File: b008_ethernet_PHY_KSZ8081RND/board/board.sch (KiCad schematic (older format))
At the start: 21 parts, among them J1 006_RMII_2x10, J2 011_GPIO_2x2, J3 009_1000BASE-T_2x5, U14 KSZ8081RND, Y1 25MhZ

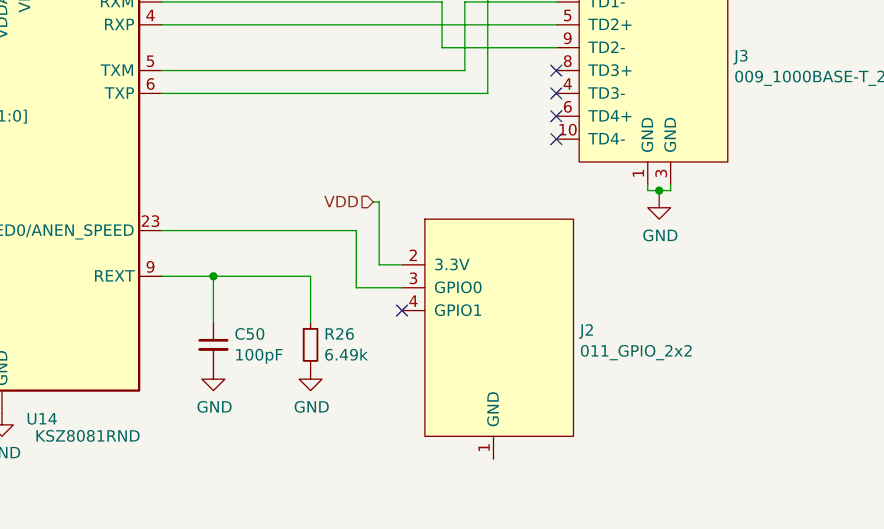
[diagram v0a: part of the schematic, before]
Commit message: added part info for silicon parts
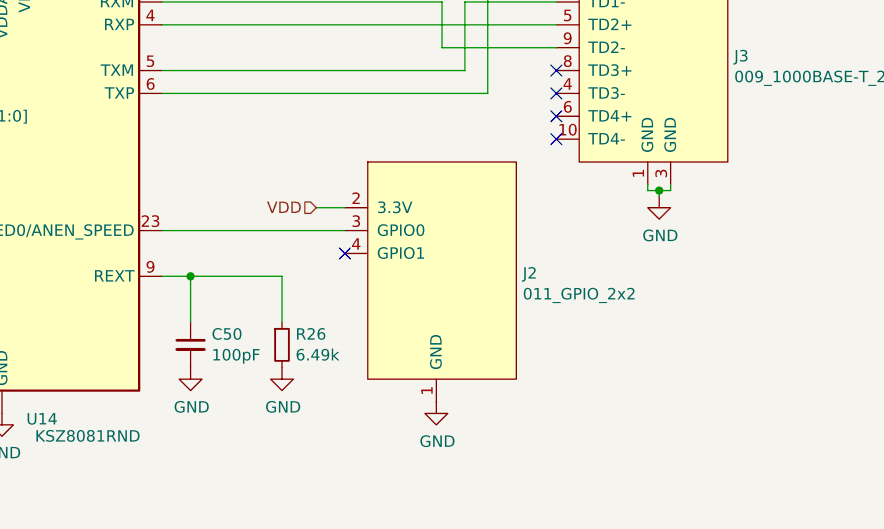
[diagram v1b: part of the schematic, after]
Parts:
- U14: MPN (none) -> KSZ8081RND
- Y1: MPN (none) -> ‎XC3065CT-ND‎
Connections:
- net GND: now also J2.1 (GND)
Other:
- moved on the sheet: C50, J2, R26
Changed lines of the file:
@@
 F 2 "Package_DFN_QFN:QFN-24-1EP_4x4mm_P0.5mm_EP2.6x2.6mm" H 7275 2200 50  0001 C CNN
 F 3 "http://ww1.microchip.com/downloads/en/DeviceDoc/00002199A.pdf" H 3625 3400 50  0001 C CNN
+F 4 "KSZ8081RND" H 5875 3200 50  0001 C CNN "MPN"
 	1    5875 3200
 	1    0    0    -1
@@
 F 2 "Crystal:Crystal_SMD_Abracon_ABM8G-4Pin_3.2x2.5mm" H 4475 4125 50  0001 C CNN
 F 3 "~" H 4475 4125 50  0001 C CNN
+F 4 "‎XC3065CT-ND‎" H 4475 4125 50  0001 C CNN "MPN"
 	1    4475 4125
 	1    0    0    -1
@@
 L Device:C_Small C50
 U 1 1 6033379D
-P 6800 3900
-F 0 "C50" H 6892 3946 50  0000 L CNN
-F 1 "100pF" H 6892 3855 50  0000 L CNN
-F 2 "Capacitor_SMD:C_0603_1608Metric" H 6800 3900 50  0001 C CNN
-F 3 "~" H 6800 3900 50  0001 C CNN
-	1    6800 3900
+P 6700 3900
+F 0 "C50" H 6792 3946 50  0000 L CNN
+F 1 "100pF" H 6792 3855 50  0000 L CNN
+F 2 "Capacitor_SMD:C_0603_1608Metric" H 6700 3900 50  0001 C CNN
+F 3 "~" H 6700 3900 50  0001 C CNN
+	1    6700 3900
 	1    0    0    -1
 $EndComp
@@
 L power:GND #PWR0144
 U 1 1 603337A3
-P 6800 4000
-F 0 "#PWR0144" H 6800 3750 50  0001 C CNN
-F 1 "GND" H 6805 3827 50  0000 C CNN
-F 2 "" H 6800 4000 50  0001 C CNN
-F 3 "" H 6800 4000 50  0001 C CNN
-	1    6800 4000
-	1    0    0    -1
-$EndComp
-Wire Wire Line
-	6575 3600 6800 3600
-Wire Wire Line
-	6800 3600 6800 3800
+P 6700 4000
+F 0 "#PWR0144" H 6700 3750 50  0001 C CNN
+F 1 "GND" H 6705 3827 50  0000 C CNN
+F 2 "" H 6700 4000 50  0001 C CNN
+F 3 "" H 6700 4000 50  0001 C CNN
+	1    6700 4000
+	1    0    0    -1
+$EndComp
+Wire Wire Line
+	6700 3600 6700 3800
 $Comp
 L Device:R_Small R26
 U 1 1 60333C7C
-P 7225 3900
-F 0 "R26" H 7284 3946 50  0000 L CNN
-F 1 "6.49k" H 7284 3855 50  0000 L CNN
-F 2 "Resistor_SMD:R_0603_1608Metric" H 7225 3900 50  0001 C CNN
-F 3 "~" H 7225 3900 50  0001 C CNN
-	1    7225 3900
+P 7100 3900
+F 0 "R26" H 7159 3946 50  0000 L CNN
+F 1 "6.49k" H 7159 3855 50  0000 L CNN
+F 2 "Resistor_SMD:R_0603_1608Metric" H 7100 3900 50  0001 C CNN
+F 3 "~" H 7100 3900 50  0001 C CNN
+	1    7100 3900
 	1    0    0    -1
 $EndComp
@@
 L power:GND #PWR0145
 U 1 1 603340ED
-P 7225 4000
-F 0 "#PWR0145" H 7225 3750 50  0001 C CNN
-F 1 "GND" H 7230 3827 50  0000 C CNN
-F 2 "" H 7225 4000 50  0001 C CNN
-F 3 "" H 7225 4000 50  0001 C CNN
-	1    7225 4000
-	1    0    0    -1
-$EndComp
-Wire Wire Line
-	7225 3800 7225 3600
-Wire Wire Line
-	7225 3600 6800 3600
-Connection ~ 6800 3600
+P 7100 4000
+F 0 "#PWR0145" H 7100 3750 50  0001 C CNN
+F 1 "GND" H 7105 3827 50  0000 C CNN
+F 2 "" H 7100 4000 50  0001 C CNN
+F 3 "" H 7100 4000 50  0001 C CNN
+	1    7100 4000
+	1    0    0    -1
+$EndComp
+Wire Wire Line
+	7100 3800 7100 3600
 $Comp
 L Device:R_Small R22
@@
 VDD
 $Comp
-L put_on_edge:011_GPIO_2x2 J2
-U 1 1 6036615C
-P 8075 3850
-F 0 "J2" H 8403 3863 50  0000 L CNN
-F 1 "011_GPIO_2x2" H 8403 3772 50  0000 L CNN
-F 2 "on_edge:on_edge_2x02_host" H 8375 4500 50  0001 C CNN
-F 3 "" H 8375 4500 50  0001 C CNN
-	1    8075 3850
-	1    0    0    -1
-$EndComp
-$Comp
 L put_on_edge:009_1000BASE-T_2x5 J3
 U 1 1 60366BF1
@@
 Wire Wire Line
 	8750 3225 8800 3225
-Wire Wire Line
-	7425 3400 7425 3650
-Wire Wire Line
-	7425 3650 7625 3650
-Wire Wire Line
-	6575 3400 7425 3400
-Text HLabel 7500 3275 0    50   Input ~ 0
+Text HLabel 7250 3300 0    50   Input ~ 0
 VDD
-Wire Wire Line
-	7500 3275 7525 3275
-Wire Wire Line
-	7525 3275 7525 3550
-Wire Wire Line
-	7525 3550 7625 3550
-NoConn ~ 7625 3750
 $Comp
 L power:GND #PWR0103
@@
 Wire Wire Line
 	4475 3950 4475 4025
+NoConn ~ 7375 3500
+$Comp
+L put_on_edge:011_GPIO_2x2 J2
+U 1 1 6036615C
+P 7825 3600
+F 0 "J2" H 8153 3613 50  0000 L CNN
+F 1 "011_GPIO_2x2" H 8153 3522 50  0000 L CNN
+F 2 "on_edge:on_edge_2x02_host" H 8125 4250 50  0001 C CNN
+F 3 "" H 8125 4250 50  0001 C CNN
+	1    7825 3600
+	1    0    0    -1
+$EndComp
+$Comp
+L power:GND #PWR?
+U 1 1 604270D0
+P 7775 4150
+F 0 "#PWR?" H 7775 3900 50  0001 C CNN
+F 1 "GND" H 7780 3977 50  0000 C CNN
+F 2 "" H 7775 4150 50  0001 C CNN
+F 3 "" H 7775 4150 50  0001 C CNN
+	1    7775 4150
+	1    0    0    -1
+$EndComp
+Wire Wire Line
+	6575 3400 7375 3400
+Wire Wire Line
+	7250 3300 7375 3300
+Connection ~ 6700 3600
+Wire Wire Line
+	6700 3600 7100 3600
+Wire Wire Line
+	6575 3600 6700 3600
 $EndSCHEMATC

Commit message: improved b008 but not done
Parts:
- J1: symbol put_on_edge:006_RMII_2x10 -> board-rescue:006_RMII_2x10-put_on_edge
- J2: footprint on_edge:on_edge_2x02_host -> on_edge:on_edge_2x05_host; symbol put_on_edge:011_GPIO_2x2 -> put_on_edge:011_GPIO
- J3: symbol put_on_edge:009_1000BASE-T_2x5 -> put_on_edge:014_100BASE-T
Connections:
- net GND: now also J3.6 (GND); no longer J3.3 (GND)
- net VDD: now also J2.9 (3.3V); no longer J2.2 (3.3V)
- net at U14.23 (LED0/ANEN_SPEED): now also J2.2 (GPIO0); no longer J2.3 (GPIO0)
- net at U14.3 (RXM): now also J3.5 (TD2-); no longer J3.9 (TD2-)
- net at U14.4 (RXP): now also J3.4 (TD2+); no longer J3.5 (TD2+)
- net at U14.5 (TXM): now also J3.3 (TD1-); no longer J3.2 (TD1-)
- net at U14.6 (TXP): now also J3.2 (TD1+); no longer J3.7 (TD1+)
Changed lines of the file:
@@
 	6575 2400 7800 2400
 $Comp
-L put_on_edge:006_RMII_2x10 J1
+L board-rescue:006_RMII_2x10-put_on_edge J1
 U 1 1 60348143
 P 1675 2650
@@
 VDD
 $Comp
-L put_on_edge:009_1000BASE-T_2x5 J3
+L put_on_edge:014_100BASE-T J3
 U 1 1 60366BF1
-P 8750 2650
-F 0 "J3" H 9078 2663 50  0000 L CNN
-F 1 "009_1000BASE-T_2x5" H 9078 2572 50  0000 L CNN
-F 2 "on_edge:on_edge_2x05_host" H 9050 3300 50  0001 C CNN
-F 3 "" H 9050 3300 50  0001 C CNN
-	1    8750 2650
-	1    0    0    -1
-$EndComp
-Wire Wire Line
-	6575 2500 8300 2500
-Wire Wire Line
-	8300 2600 7800 2600
+P 9650 2650
+F 0 "J3" H 9978 2663 50  0000 L CNN
+F 1 "009_1000BASE-T_2x5" H 9978 2572 50  0000 L CNN
+F 2 "on_edge:on_edge_2x05_host" H 9950 3300 50  0001 C CNN
+F 3 "" H 9950 3300 50  0001 C CNN
+	1    9650 2650
+	1    0    0    -1
+$EndComp
 Wire Wire Line
 	7800 2600 7800 2400
@@
 	7900 2700 7900 2400
 Wire Wire Line
-	7900 2400 8300 2400
-Wire Wire Line
 	6575 2700 7900 2700
 Wire Wire Line
 	8000 2800 8000 2300
 Wire Wire Line
-	8000 2300 8300 2300
-Wire Wire Line
 	6575 2800 8000 2800
-NoConn ~ 8300 2700
-NoConn ~ 8300 2800
-NoConn ~ 8300 2900
-NoConn ~ 8300 3000
 $Comp
 L power:GND #PWR0102
 U 1 1 60385EA1
-P 8750 3250
-F 0 "#PWR0102" H 8750 3000 50  0001 C CNN
-F 1 "GND" H 8755 3077 50  0000 C CNN
-F 2 "" H 8750 3250 50  0001 C CNN
-F 3 "" H 8750 3250 50  0001 C CNN
-	1    8750 3250
-	1    0    0    -1
-$EndComp
-Wire Wire Line
-	8700 3200 8700 3225
-Wire Wire Line
-	8700 3225 8750 3225
-Wire Wire Line
-	8800 3225 8800 3200
-Wire Wire Line
-	8750 3250 8750 3225
-Connection ~ 8750 3225
-Wire Wire Line
-	8750 3225 8800 3225
-Text HLabel 7250 3300 0    50   Input ~ 0
+P 9650 3250
+F 0 "#PWR0102" H 9650 3000 50  0001 C CNN
+F 1 "GND" H 9655 3077 50  0000 C CNN
+F 2 "" H 9650 3250 50  0001 C CNN
+F 3 "" H 9650 3250 50  0001 C CNN
+	1    9650 3250
+	1    0    0    -1
+$EndComp
+Wire Wire Line
+	9600 3200 9600 3225
+Wire Wire Line
+	9600 3225 9650 3225
+Wire Wire Line
+	9700 3225 9700 3200
+Wire Wire Line
+	9650 3250 9650 3225
+Connection ~ 9650 3225
+Wire Wire Line
+	9650 3225 9700 3225
+Text HLabel 7825 4000 0    50   Input ~ 0
 VDD
 $Comp
@@
 Wire Wire Line
 	4475 3950 4475 4025
-NoConn ~ 7375 3500
-$Comp
-L put_on_edge:011_GPIO_2x2 J2
+NoConn ~ 7950 3500
+$Comp
+L put_on_edge:011_GPIO J2
 U 1 1 6036615C
-P 7825 3600
-F 0 "J2" H 8153 3613 50  0000 L CNN
-F 1 "011_GPIO_2x2" H 8153 3522 50  0000 L CNN
-F 2 "on_edge:on_edge_2x02_host" H 8125 4250 50  0001 C CNN
-F 3 "" H 8125 4250 50  0001 C CNN
-	1    7825 3600
-	1    0    0    -1
-$EndComp
-$Comp
-L power:GND #PWR?
+P 8400 3750
+F 0 "J2" H 8728 3763 50  0000 L CNN
+F 1 "011_GPIO_2x2" H 8728 3672 50  0000 L CNN
+F 2 "on_edge:on_edge_2x05_host" H 8700 4400 50  0001 C CNN
+F 3 "" H 8700 4400 50  0001 C CNN
+	1    8400 3750
+	1    0    0    -1
+$EndComp
+$Comp
+L power:GND #PWR0105
 U 1 1 604270D0
-P 7775 4150
-F 0 "#PWR?" H 7775 3900 50  0001 C CNN
-F 1 "GND" H 7780 3977 50  0000 C CNN
-F 2 "" H 7775 4150 50  0001 C CNN
-F 3 "" H 7775 4150 50  0001 C CNN
-	1    7775 4150
-	1    0    0    -1
-$EndComp
-Wire Wire Line
-	6575 3400 7375 3400
-Wire Wire Line
-	7250 3300 7375 3300
+P 8350 4300
+F 0 "#PWR0105" H 8350 4050 50  0001 C CNN
+F 1 "GND" H 8355 4127 50  0000 C CNN
+F 2 "" H 8350 4300 50  0001 C CNN
+F 3 "" H 8350 4300 50  0001 C CNN
+	1    8350 4300
+	1    0    0    -1
+$EndComp
+Wire Wire Line
+	7825 4000 7950 4000
 Connection ~ 6700 3600
 Wire Wire Line
@@
 Wire Wire Line
 	6575 3600 6700 3600
+Wire Wire Line
+	8000 2300 9200 2300
+Wire Wire Line
+	7900 2400 9200 2400
+Wire Wire Line
+	6575 2500 9200 2500
+Wire Wire Line
+	7800 2600 9200 2600
+Wire Wire Line
+	6575 3400 7950 3400
+NoConn ~ 7950 3900
+NoConn ~ 7950 3800
+NoConn ~ 7950 3700
+NoConn ~ 7950 3600
 $EndSCHEMATC
